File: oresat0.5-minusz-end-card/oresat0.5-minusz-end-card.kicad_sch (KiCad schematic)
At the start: 0 parts

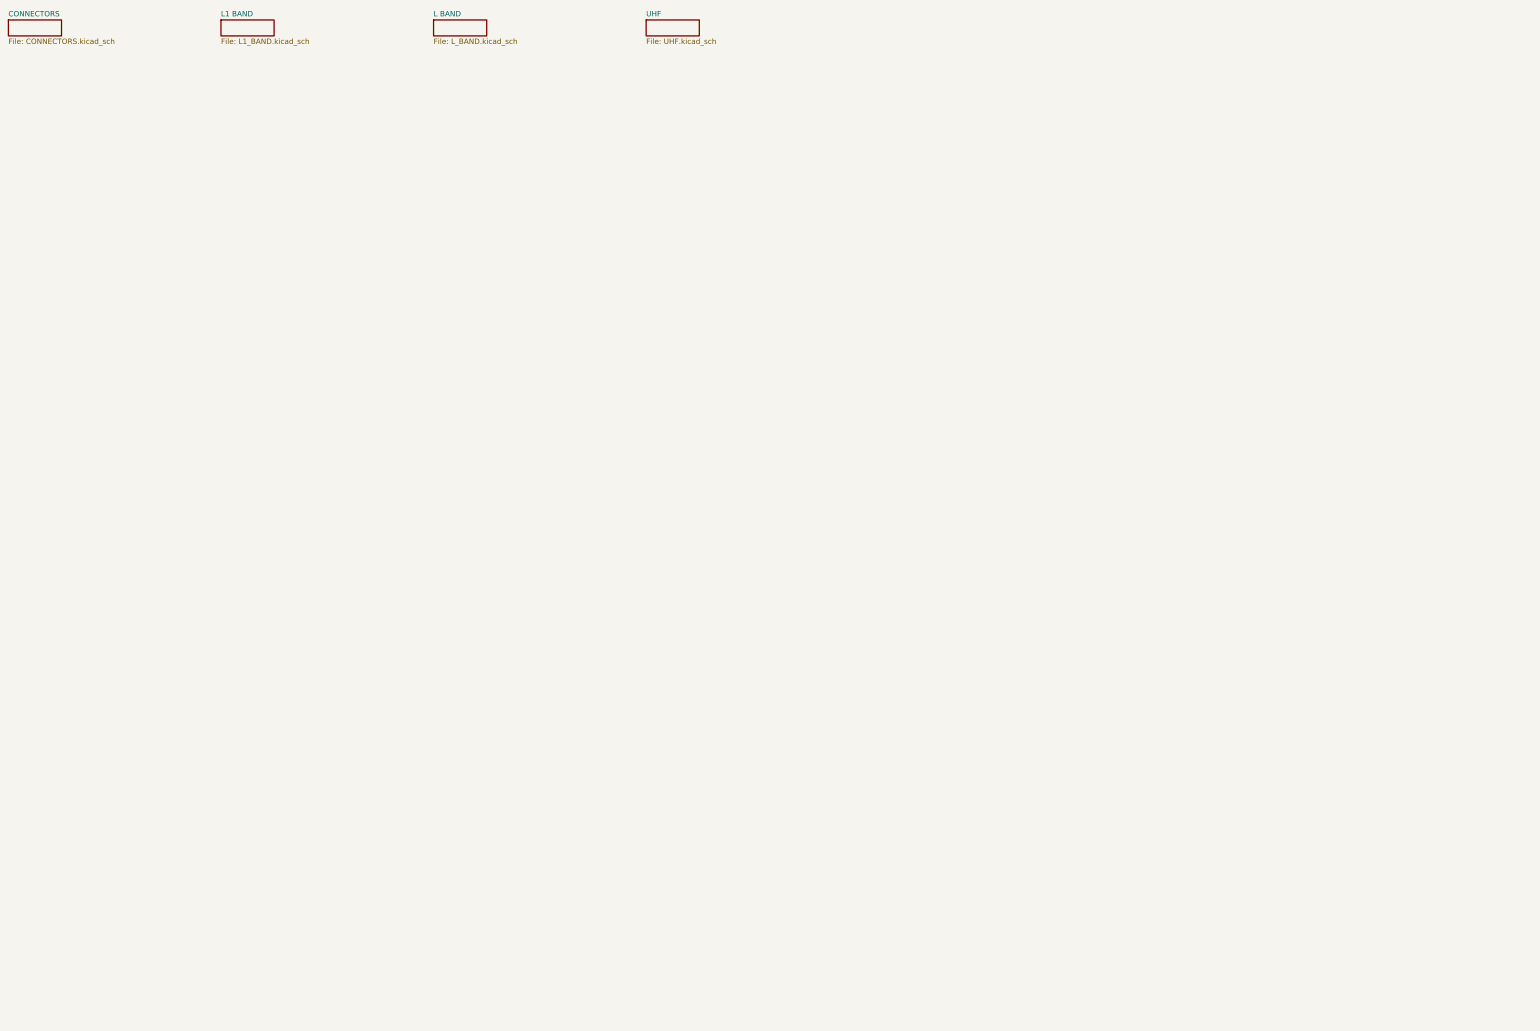
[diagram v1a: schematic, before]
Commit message: Fixed up OreSat0.5 -Z end card: Added hole for U.FL connector to get to GPS antnena, fixed library paths which seemed broken, replaced older EAGLE files too, fixed schematic/board disconnect with ref designators, cleaned up ERCs and DRCs.
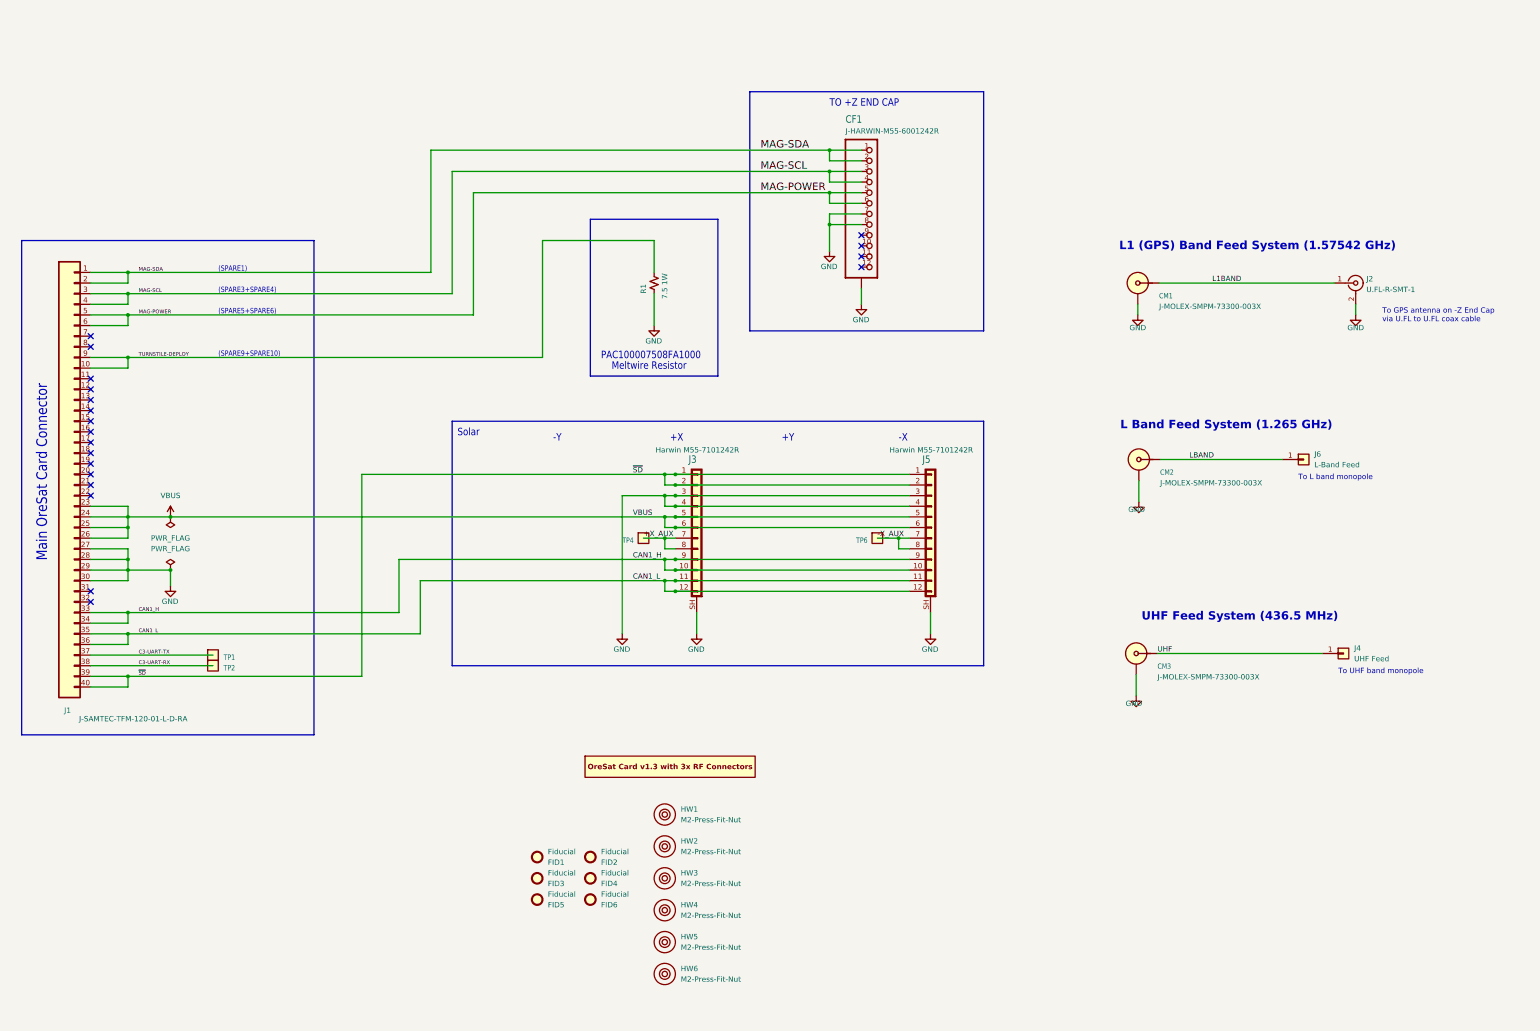
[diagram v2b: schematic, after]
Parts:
- added CF1: J-HARWIN-M55-6001242R, oresat-connectors:J-Harwin-M55-60X1242R, symbol oresat-connectors:J-HARWIN-M55-6001242R
- added CM1, CM2, CM3: J-MOLEX-SMPM-73300-003X, oresat-connectors:J-MOLEX-SMPM-073300-002X, symbol oresat-connectors:J-MOLEX-SMPM-73300-002X
- added FID1, FID2, FID3, FID4, FID5, FID6: Fiducial, Fiducial:Fiducial_1mm_Mask2mm, symbol Mechanical:Fiducial
- added HW1, HW2, HW3, HW4, HW5, HW6: M2-Press-Fit-Nut, oresat-misc:M2-Press-Fit-Nut, symbol oresat-misc:M2-Press-Fit-Nut
- added J1: J-SAMTEC-TFM-120-01-L-D-RA, oresat-connectors:J-SAMTEC-TFM-120-X1-XXX-D-RA, symbol oresat-connectors:J-SAMTEC-TFM-120-01-L-D-RA
- added J2: U.FL-R-SMT-1, Connector_Coaxial:U.FL_Hirose_U.FL-R-SMT-1_Vertical, symbol Connector:Conn_Coaxial
- added J3, J5: Harwin M55-7101242R, oresat-connectors:J-Harwin-M55-7101242R, symbol oresat-connectors:Harwin M55-7101242R
- added J4: UHF Feed, Connector_Pin:Pin_D1.0mm_L10.0mm, symbol Connector_Generic:Conn_01x01
- added J6: L-Band Feed, Connector_Pin:Pin_D1.0mm_L10.0mm, symbol Connector_Generic:Conn_01x01
- added PCB1: ORESAT-CARD-V1.3-GENERIC-3RF, oresat-pcbs:ORESAT-CARD-V1.3-3RF, symbol oresat-pcbs:ORESAT-CARD-V1.3-3RF
- added R1: 7.5 1W, oresat-passives:R-PAC100-FOR-MELTWIRE, symbol Device:R_Small_US
- added TP1, TP2, TP4, TP6: TEST-POINT-LARGE-SQUARE, oresat-misc:TestPoint-0.75mm-th, symbol oresat-misc:Test-Point-0.75mm-th
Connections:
- new net +X_AUX: J3.7 (Pin_7), J3.8 (Pin_8), TP4.1
- new net -X_AUX: J5.7 (Pin_7), J5.8 (Pin_8), TP6.1
- new net C3-UART-RX: J1.38, TP2.1
- new net C3-UART-TX: J1.37, TP1.1
- new net CAN1_H: J1.33, J1.34, J3.10 (Pin_10), J3.9 (Pin_9), J5.10 (Pin_10), J5.9 (Pin_9)
- new net CAN1_L: J1.35, J1.36, J3.11 (Pin_11), J3.12 (Pin_12), J5.11 (Pin_11), J5.12 (Pin_12)
- new net GND: CF1.7, CF1.8, CF1.SH (SHIELD), CM1.SHLD, CM2.SHLD, CM3.SHLD, J1.27, J1.28, J1.29, J1.30, J2.2 (Ext), J3.3 (Pin_3), J3.4 (Pin_4), J3.SH (Shield), J5.3 (Pin_3), J5.4 (Pin_4), J5.SH (Shield), R1.2
- new net L1BAND: CM1.SIG, J2.1 (In)
- new net LBAND: CM2.SIG, J6.1 (Pin_1)
- new net MAG-POWER: CF1.5, CF1.6, J1.5, J1.6
- new net MAG-SCL: CF1.3, CF1.4, J1.3, J1.4
- new net MAG-SDA: CF1.1, CF1.2, J1.1, J1.2
- new net TURNSTILE-DEPLOY: J1.10, J1.9, R1.1
- new net UHF: CM3.SIG, J4.1 (Pin_1)
- new net VBUS: J1.23, J1.24, J1.25, J1.26, J3.5 (Pin_5), J3.6 (Pin_6), J5.5 (Pin_5), J5.6 (Pin_6)
- new net ~{SD}: J1.39, J1.40, J3.1 (Pin_1), J3.2 (Pin_2), J5.1 (Pin_1), J5.2 (Pin_2)
- no-connect marks 0 -> 20
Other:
- removed sheet CONNECTORS
- removed sheet L BAND
- removed sheet L1 BAND
- removed sheet UHF
- note added: "(SPARE1)"
- note added: "(SPARE3+SPARE4)"
- note added: "(SPARE5+SPARE6)"
- note added: "(SPARE9+SPARE10)"
- note added: "+X"
- note added: "+Y"
- note added: "-X"
- note added: "-Y"
- note added: "L Band Feed System (1.265 GHz)"
- note added: "L1 (GPS) Band Feed System (1.57542 GHz)"
- note added: "Main OreSat Card Connector"
- note added: "Meltwire Resistor"
- note added: "PAC100007508FA1000"
- note added: "Solar"
- note added: "TO +Z END CAP"
- note added: "To GPS antenna on -Z End Cap via U.FL to U.FL coax cable"
- note added: "To L band monopole"
- note added: "To UHF band monopole"
- note added: "UHF Feed System (436.5 MHz)"
- title: +Z End Card w/ Turnstile -> OreSat0.5 -Z End Card

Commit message: Moves antenna connection from large vias to slots so we don't need an a lead on the 1/4 inch tape measure antennas.
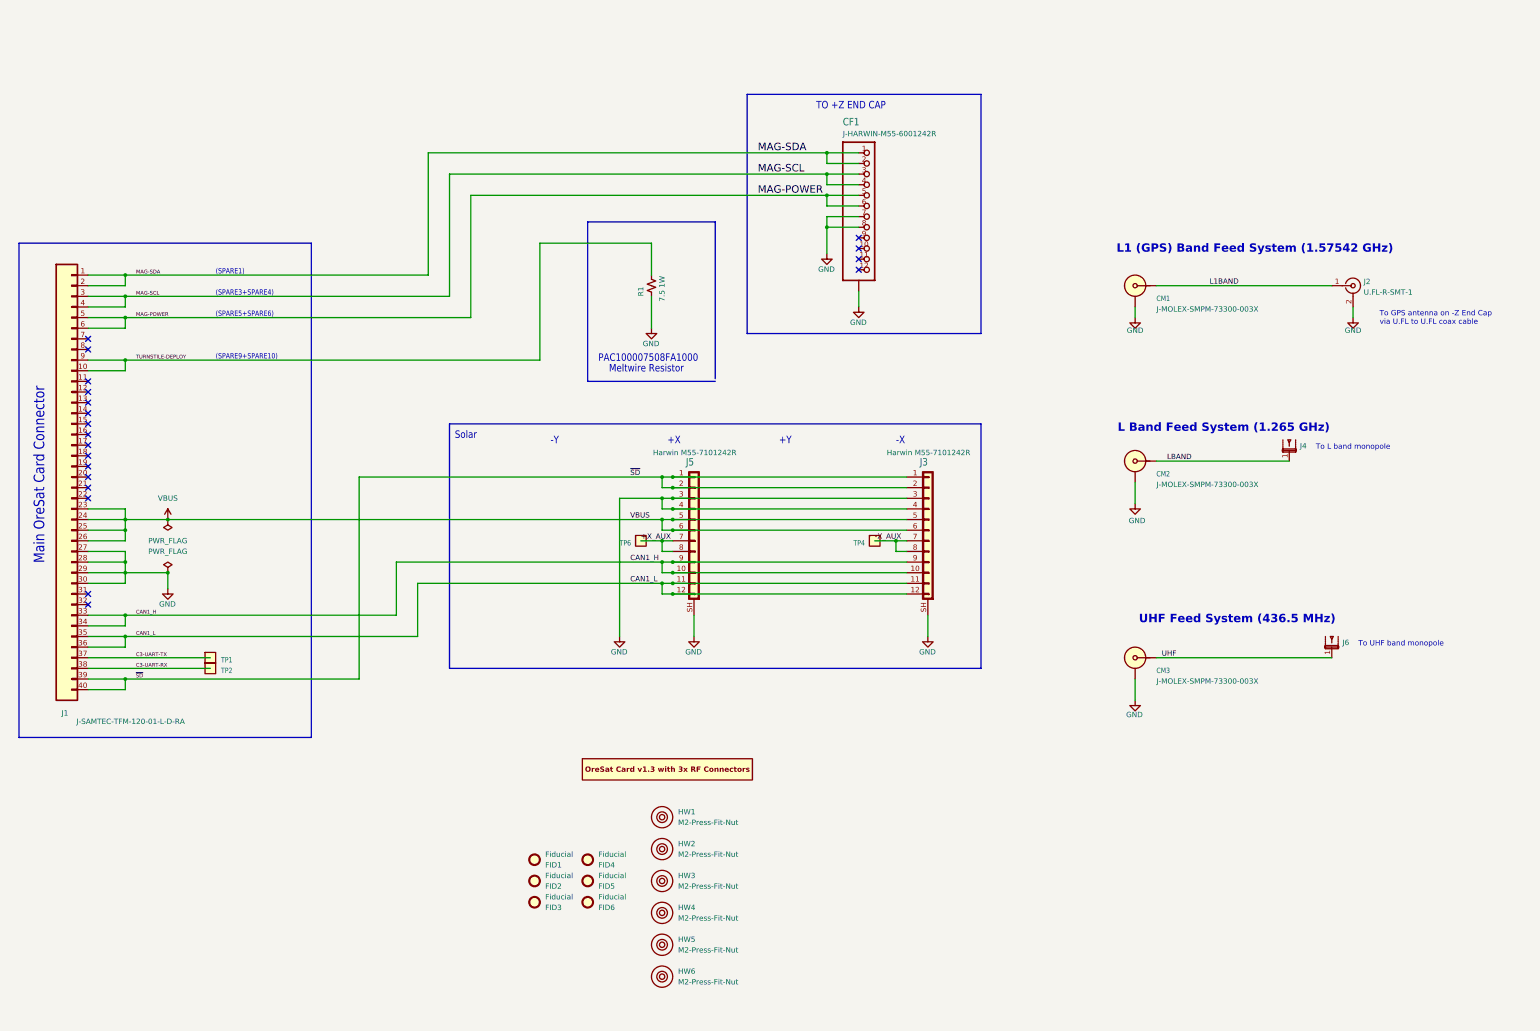
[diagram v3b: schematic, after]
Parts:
- removed J4: UHF Feed, Connector_Pin:Pin_D1.0mm_L10.0mm, symbol Connector_Generic:Conn_01x01
- removed J6: L-Band Feed, Connector_Pin:Pin_D1.0mm_L10.0mm, symbol Connector_Generic:Conn_01x01
- added J4, J6: ~, oresat-misc:tape-measure-slot-antenna, symbol oresat-misc:tape-measure-antenna
- renumbered FID3 to FID2, FID5 to FID3, FID2 to FID4, FID4 to FID5, J5 to J3, J3 to J5, TP6 to TP4, TP4 to TP6
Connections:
- net LBAND: now also J4.1
- net UHF: now also J6.1
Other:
- moved on the sheet: CF1, CM1, CM2, CM3, FID1, FID2, FID3, FID4, FID5, FID6, HW1, HW2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

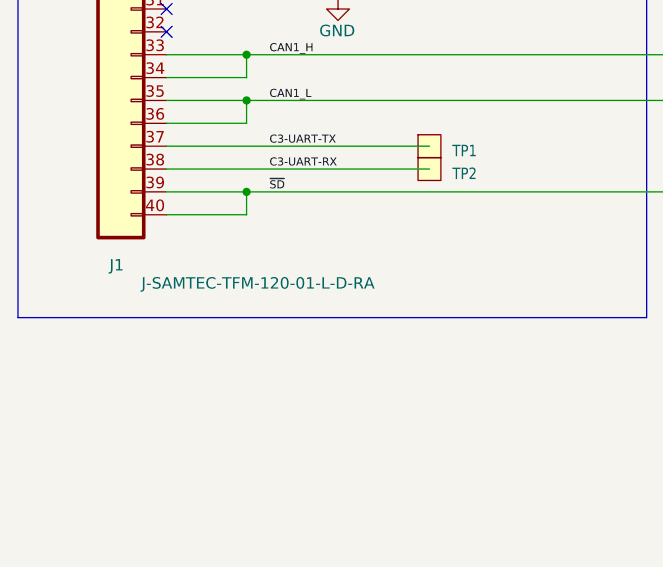
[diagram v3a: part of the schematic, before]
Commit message: Updated date and unecessary polish on planes, including fillets and just more planes with more vias.
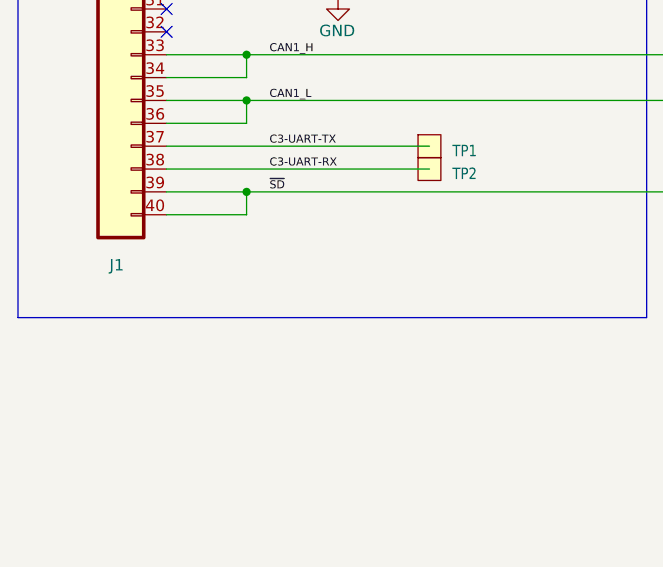
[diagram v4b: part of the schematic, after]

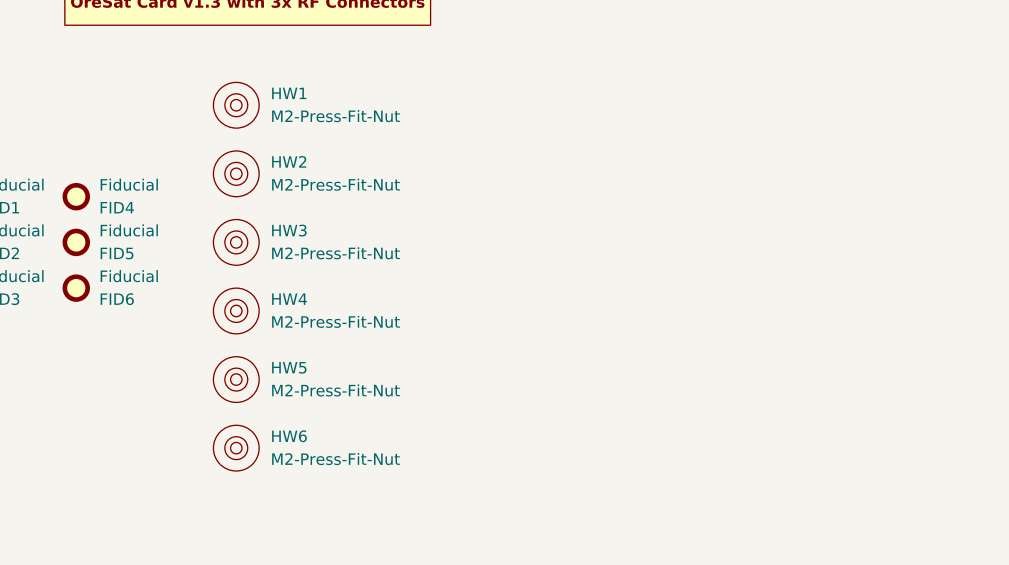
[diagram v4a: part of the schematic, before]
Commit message: Added M2 fastener holes back into the -Z end card. Rev'd to v1.4.
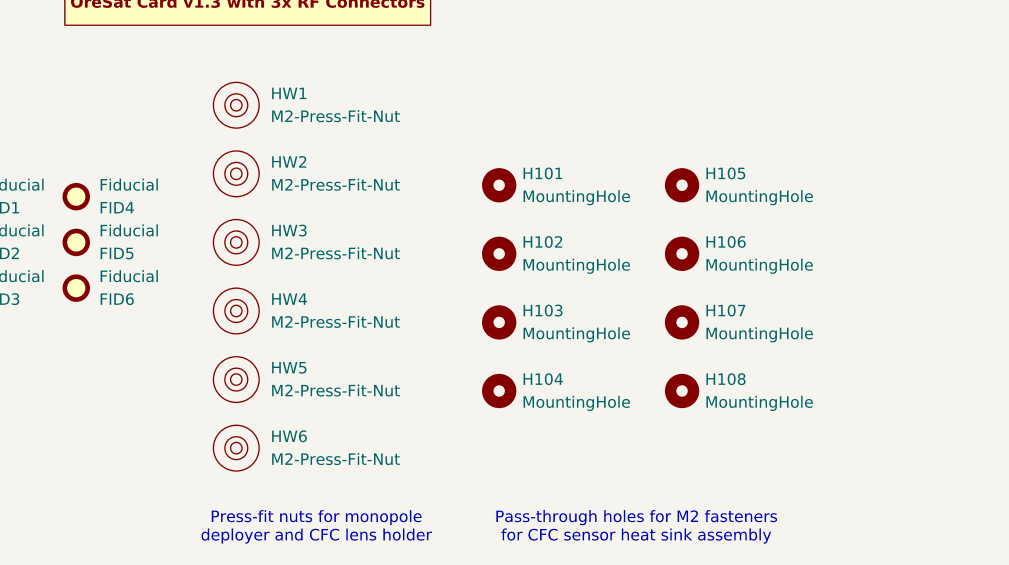
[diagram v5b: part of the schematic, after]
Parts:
- added H101, H102, H103, H104, H105, H106, H107, H108: MountingHole, MountingHole:MountingHole_5mm, symbol Mechanical:MountingHole
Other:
- note added: "Pass-through holes for M2 fasteners for CFC sensor heat sink assembly"
- note added: "Press-fit nuts for monopole deployer and CFC lens holder"
